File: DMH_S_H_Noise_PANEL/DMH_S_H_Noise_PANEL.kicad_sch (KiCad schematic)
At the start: 5 parts, among them J0 Panel_GND_Solder_Wire_Pad

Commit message: Created front panel
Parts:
- added H10: Slw In, SynthStuff:Jack_6.35mm_Cutout_v3, symbol SynthStuff:MountingHole_Jack6.35mm_v2
- added H11: S&H Out, SynthStuff:Jack_6.35mm_Cutout_Output_v6, symbol SynthStuff:MountingHole_Jack6.35mm_Output_v2
- added H12: Slw Out, SynthStuff:Jack_6.35mm_Cutout_Output_v6, symbol SynthStuff:MountingHole_Jack6.35mm_Output_v2
- added H13: White, SynthStuff:Jack_6.35mm_Cutout_Output_v6, symbol SynthStuff:MountingHole_Jack6.35mm_Output_v2
- added H14: Pink, SynthStuff:Jack_6.35mm_Cutout_Output_v6, symbol SynthStuff:MountingHole_Jack6.35mm_Output_v2
- added H15: Blue, SynthStuff:Jack_6.35mm_Cutout_Output_v6, symbol SynthStuff:MountingHole_Jack6.35mm_Output_v2
- added H5: Rate, SynthStuff:Pot_Cutout_Large_v2, symbol SynthStuff:MountingHole_Pot
- added H6: CV Amount, SynthStuff:Pot_Cutout_Small, symbol SynthStuff:MountingHole_Pot
- added H7: Slew, SynthStuff:Pot_Cutout_Small, symbol SynthStuff:MountingHole_Pot
- added H8: CV In, SynthStuff:Jack_6.35mm_Cutout_v3, symbol SynthStuff:MountingHole_Jack6.35mm_v2
- added H9: Clk In, SynthStuff:Jack_6.35mm_Cutout_v3, symbol SynthStuff:MountingHole_Jack6.35mm_v2
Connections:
- net GND: now also H10.1, H11.1, H12.1, H13.1, H14.1, H15.1, H5.1, H6.1, H7.1, H8.1, H9.1

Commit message: Completed circuit
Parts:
- H6: value CV Amount -> Input Level
- H8: value CV In -> Input
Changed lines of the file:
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@@
 			)
 		)
-		(property "Value" "CV Amount"
+		(property "Value" "Input Level"
 			(at 66.04 152.3999 0)
 			(effects
@@
 			)
 		)
-		(property "Value" "CV In"
+		(property "Value" "Input"
 			(at 66.04 190.4999 0)
 			(effects

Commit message: Added Rate LED to the panel
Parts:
- added H16: Rate LED, SynthStuff:MountingHole_LED_3mm, symbol Mechanical:MountingHole
- H5: footprint SynthStuff:Pot_Cutout_Large_v2 -> SynthStuff:Pot_Cutout_Medium_v2
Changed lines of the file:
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@@
 			)
 		)
-		(property "Footprint" "SynthStuff:Pot_Cutout_Large_v2"
+		(property "Footprint" "SynthStuff:Pot_Cutout_Medium_v2"
 			(at 88.9 140.97 0)
 			(effects
@@
 					(unit 1)
 				)
+			)
+		)
+	)
+	(symbol
+		(lib_id "Mechanical:MountingHole")
+		(at 88.9 127 0)
+		(unit 1)
+		(exclude_from_sim yes)
+		(in_bom no)
+		(on_board yes)
+		(dnp no)
+		(fields_autoplaced yes)
+		(property "Reference" "H16"
+			(at 91.44 125.7299 0)
+			(effects
+				(font
+					(size 1.27 1.27)
+				)
+				(justify left)
+			)
+		)
+		(property "Value" "Rate LED"
+			(at 91.44 128.2699 0)
+			(effects
+				(font
+					(size 1.27 1.27)
+				)
+				(justify left)
+			)
+		)
+		(property "Footprint" "SynthStuff:MountingHole_LED_3mm"
+			(at 88.9 127 0)
+			(effects
+				(font
+					(size 1.27 1.27)
+				)
+				(hide yes)
+			)
+		)
+		(property "Datasheet" "~"
+			(at 88.9 127 0)
+			(effects
+				(font
+					(size 1.27 1.27)
+				)
+				(hide yes)
+			)
+		)
+		(property "Description" "Mounting Hole without connection"
+			(at 88.9 127 0)
+			(effects
+				(font
+					(size 1.27 1.27)
+				)
+				(hide yes)
+			)
+		)
+		(instances
+			(project ""
+				(path "/a552705f-a9fe-462e-9913-5cfcc08b233c"
+					(reference "H16")
+					(unit 1)
+				)

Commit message: Manual trigger panel experiments ongoing
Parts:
- added H17: Switch, SynthStuff:MX_switch_Cutout, symbol Mechanical:MountingHole
- H10: value Slw In -> Slew In
- H11: value S&H Out -> S&H
- H12: value Slw Out -> Slew
- H9: value Clk In -> Clock
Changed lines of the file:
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@@
 			)
 		)
-		(property "Value" "Slw In"
+		(property "Value" "Slew In"
 			(at 116.84 190.4999 0)
 			(effects
@@
 			)
 		)
-		(property "Value" "Slw Out"
+		(property "Value" "Slew"
 			(at 66.04 203.1999 0)
 			(effects
@@
 			)
 		)
-		(property "Value" "S&H Out"
+		(property "Value" "S&H"
 			(at 40.64 203.1999 0)
 			(effects
@@
 				(path "/a552705f-a9fe-462e-9913-5cfcc08b233c"
 					(reference "H8")
+					(unit 1)
+				)
+			)
+		)
+	)
+	(symbol
+		(lib_id "Mechanical:MountingHole")
+		(at 88.9 228.6 0)
+		(unit 1)
+		(exclude_from_sim yes)
+		(in_bom no)
+		(on_board yes)
+		(dnp no)
+		(fields_autoplaced yes)
+		(property "Reference" "H17"
+			(at 91.44 227.3299 0)
+			(effects
+				(font
+					(size 1.27 1.27)
+				)
+				(justify left)
+			)
+		)
+		(property "Value" "Switch"
+			(at 91.44 229.8699 0)
+			(effects
+				(font
+					(size 1.27 1.27)
+				)
+				(justify left)
+			)
+		)
+		(property "Footprint" "SynthStuff:MX_switch_Cutout"
+			(at 88.9 228.6 0)
+			(effects
+				(font
+					(size 1.27 1.27)
+				)
+				(hide yes)
+			)
+		)
+		(property "Datasheet" "~"
+			(at 88.9 228.6 0)
+			(effects
+				(font
+					(size 1.27 1.27)
+				)
+				(hide yes)
+			)
+		)
+		(property "Description" "Mounting Hole without connection"
+			(at 88.9 228.6 0)
+			(effects
+				(font
+					(size 1.27 1.27)
+				)
+				(hide yes)
+			)
+		)
+		(instances
+			(project ""
+				(path "/a552705f-a9fe-462e-9913-5cfcc08b233c"
+					(reference "H17")
 					(unit 1)
 				)
@@
 			)
 		)
-		(property "Value" "Clk In"
+		(property "Value" "Clock"
 			(at 91.44 190.4999 0)
 			(effects

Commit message: Finished front panel
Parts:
- added H18: Trigger Source, SynthStuff:Toggle_Switch_Cutout, symbol SynthStuff:MountingHole_ToggleSwitch
- H17: value Switch -> Manual Trigger
- H6, H7: footprint SynthStuff:Pot_Cutout_Small -> SynthStuff:Pot_Cutout_Tiny
- H9: value Clock -> Ext.Clk
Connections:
- net GND: now also H18.1
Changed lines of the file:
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@@
+	)
+	(junction
+		(at 34.29 196.85)
+		(diameter 0)
+		(color 0 0 0 0)
 	)
 	(junction
@@
 	(wire
 		(pts
+			(xy 34.29 181.61) (xy 34.29 196.85)
+		)
+		(stroke
+			(width 0)
+			(type default)
+		)
+	)
+	(wire
+		(pts
 			(xy 114.3 160.02) (xy 88.9 160.02)
 		)
@@
 			)
 		)
-		(property "Footprint" "SynthStuff:Pot_Cutout_Small"
+		(property "Footprint" "SynthStuff:Pot_Cutout_Tiny"
 			(at 63.5 153.67 0)
 			(effects
@@
 			)
 		)
-		(property "Footprint" "SynthStuff:Pot_Cutout_Small"
+		(property "Footprint" "SynthStuff:Pot_Cutout_Tiny"
 			(at 114.3 153.67 0)
 			(effects
@@
 	)
 	(symbol
+		(lib_id "SynthStuff:MountingHole_ToggleSwitch")
+		(at 34.29 177.8 0)
+		(unit 1)
+		(exclude_from_sim yes)
+		(in_bom no)
+		(on_board yes)
+		(dnp no)
+		(fields_autoplaced yes)
+		(property "Reference" "H18"
+			(at 36.83 175.2599 0)
+			(effects
+				(font
+					(size 1.27 1.27)
+				)
+				(justify left)
+			)
+		)
+		(property "Value" "Trigger Source"
+			(at 36.83 177.7999 0)
+			(effects
+				(font
+					(size 1.27 1.27)
+				)
+				(justify left)
+			)
+		)
+		(property "Footprint" "SynthStuff:Toggle_Switch_Cutout"
+			(at 34.29 177.8 0)
+			(effects
+				(font
+					(size 1.27 1.27)
+				)
+				(hide yes)
+			)
+		)
+		(property "Datasheet" "~"
+			(at 34.29 177.8 0)
+			(effects
+				(font
+					(size 1.27 1.27)
+				)
+				(hide yes)
+			)
+		)
+		(property "Description" "Toggle Switch Mounting Hole"
+			(at 36.83 180.3399 0)
+			(effects
+				(font
+					(size 1.27 1.27)
+				)
+				(justify left)
+			)
+		)
+		(pin "1"
+		)
+		(instances
+			(project ""
+				(path "/a552705f-a9fe-462e-9913-5cfcc08b233c"
+					(reference "H18")
+					(unit 1)
+				)
+			)
+		)
+	)
+	(symbol
 		(lib_id "SynthStuff:MountingHole_Rails")
 		(at 27.94 265.43 0)
@@
 			)
 		)
-		(property "Value" "Switch"
+		(property "Value" "Manual Trigger"
 			(at 91.44 229.8699 0)
 			(effects
@@
 			)
 		)
-		(property "Value" "Clock"
+		(property "Value" "Ext.Clk"
 			(at 91.44 190.4999 0)
 			(effects

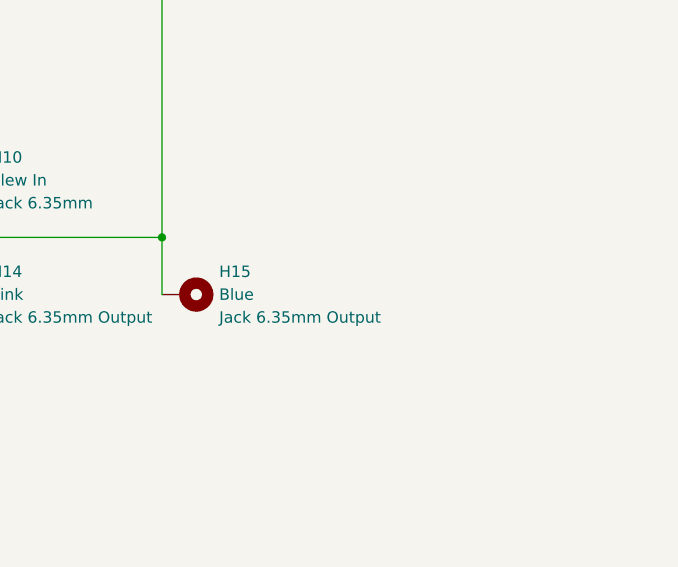
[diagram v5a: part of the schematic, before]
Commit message: Added clock output
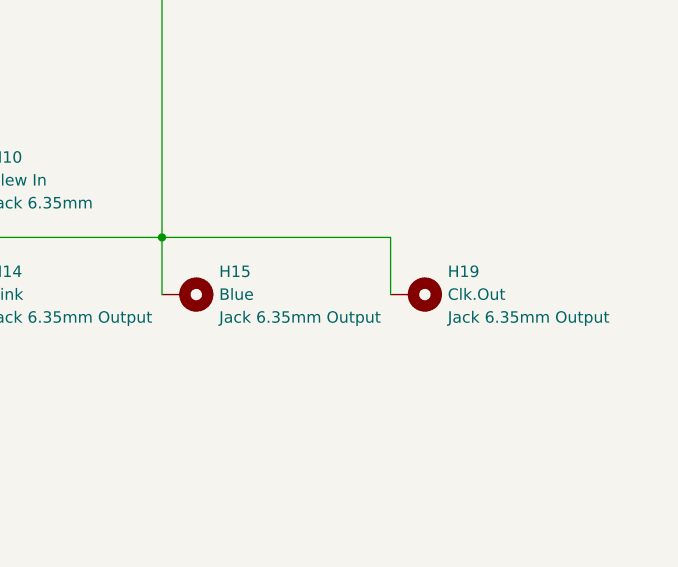
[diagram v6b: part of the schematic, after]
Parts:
- added H19: Clk.Out, SynthStuff:Jack_6.35mm_Cutout_Output_v6, symbol SynthStuff:MountingHole_Jack6.35mm_Output_v2
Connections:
- net GND: now also H19.1
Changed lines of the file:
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@@
+	(wire
+		(pts
+			(xy 161.29 203.2) (xy 161.29 196.85)
+		)
+		(stroke
+			(width 0)
+			(type default)
+		)
+	)
 	(wire
 		(pts
@@
 		(pts
 			(xy 110.49 196.85) (xy 135.89 196.85)
+		)
+		(stroke
+			(width 0)
+			(type default)
+		)
+	)
+	(wire
+		(pts
+			(xy 161.29 196.85) (xy 135.89 196.85)
 		)
 		(stroke
@@
 					(unit 1)
 				)
+			)
+		)
+	)
+	(symbol
+		(lib_id "SynthStuff:MountingHole_Jack6.35mm_Output_v2")
+		(at 165.1 203.2 0)
+		(unit 1)
+		(exclude_from_sim yes)
+		(in_bom no)
+		(on_board yes)
+		(dnp no)
+		(fields_autoplaced yes)
+		(property "Reference" "H19"
+			(at 167.64 200.6599 0)
+			(effects
+				(font
+					(size 1.27 1.27)
+				)
+				(justify left)
+			)
+		)
+		(property "Value" "Clk.Out"
+			(at 167.64 203.1999 0)
+			(effects
+				(font
+					(size 1.27 1.27)
+				)
+				(justify left)
+			)
+		)
+		(property "Footprint" "SynthStuff:Jack_6.35mm_Cutout_Output_v6"
+			(at 165.1 203.2 0)
+			(effects
+				(font
+					(size 1.27 1.27)
+				)
+				(hide yes)
+			)
+		)
+		(property "Datasheet" "~"
+			(at 165.1 203.2 0)
+			(effects
+				(font
+					(size 1.27 1.27)
+				)
+				(hide yes)
+			)
+		)
+		(property "Description" "Jack 6.35mm Output"
+			(at 167.64 205.7399 0)
+			(effects
+				(font
+					(size 1.27 1.27)
+				)
+				(justify left)
+			)
+		)
+		(pin "1"
+		)
+		(instances
+			(project "DMH_S_H_Noise_PANEL"
+				(path "/a552705f-a9fe-462e-9913-5cfcc08b233c"
+					(reference "H19")
+					(unit 1)
+				)

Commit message: Generated BoM
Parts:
- H17, H5, H6, H7: now in the parts list
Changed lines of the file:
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@@
 		(unit 1)
 		(exclude_from_sim yes)
-		(in_bom no)
+		(in_bom yes)
 		(on_board yes)
 		(dnp no)
@@
 		(unit 1)
 		(exclude_from_sim yes)
-		(in_bom no)
+		(in_bom yes)
 		(on_board yes)
 		(dnp no)
@@
 		(unit 1)
 		(exclude_from_sim yes)
-		(in_bom no)
+		(in_bom yes)
 		(on_board yes)
 		(dnp no)
@@
 		(unit 1)
 		(exclude_from_sim yes)
-		(in_bom no)
-		(on_board yes)
-		(dnp no)
+		(in_bom yes)
+		(on_board yes)
+		(dnp no)
